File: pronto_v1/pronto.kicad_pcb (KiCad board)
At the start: 2 copper layers, 53.3 x 81.3 mm, 480 parts

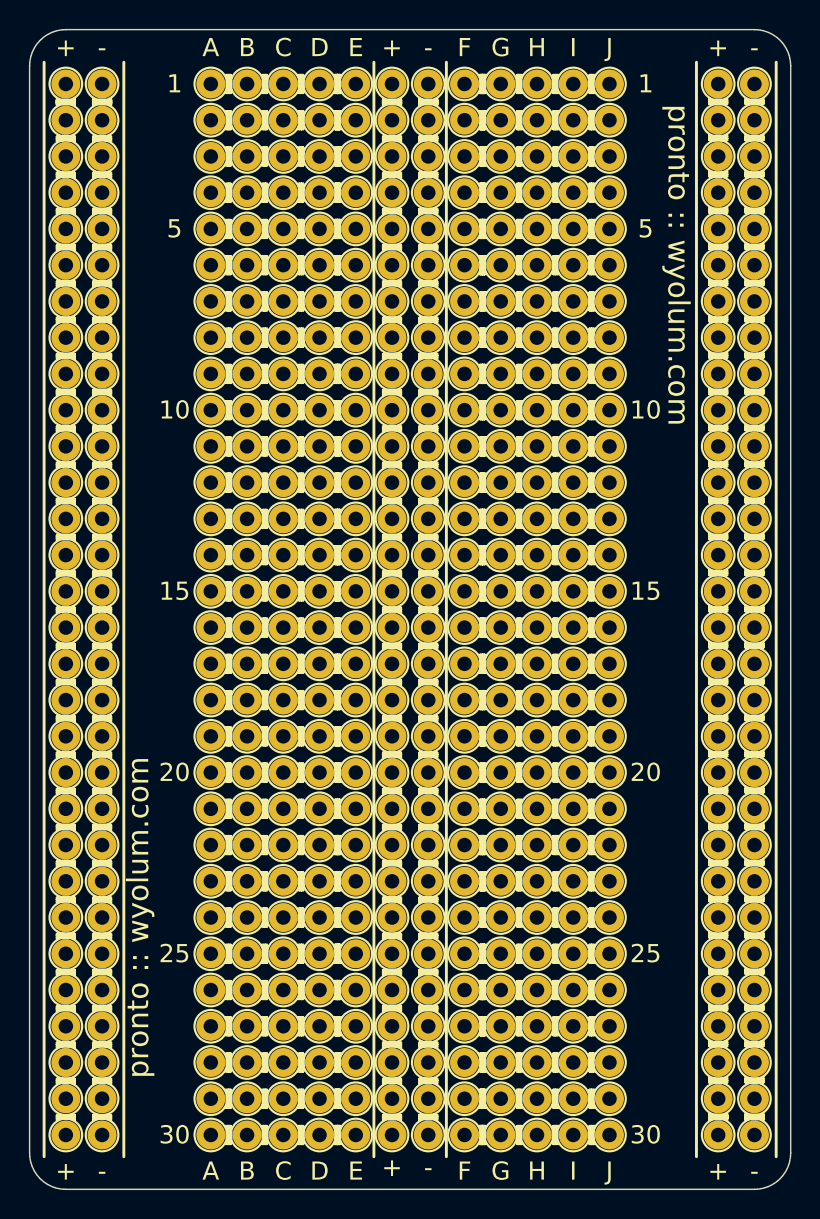
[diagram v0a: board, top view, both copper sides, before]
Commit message: updated Maker's Asylum version and added Makerville version
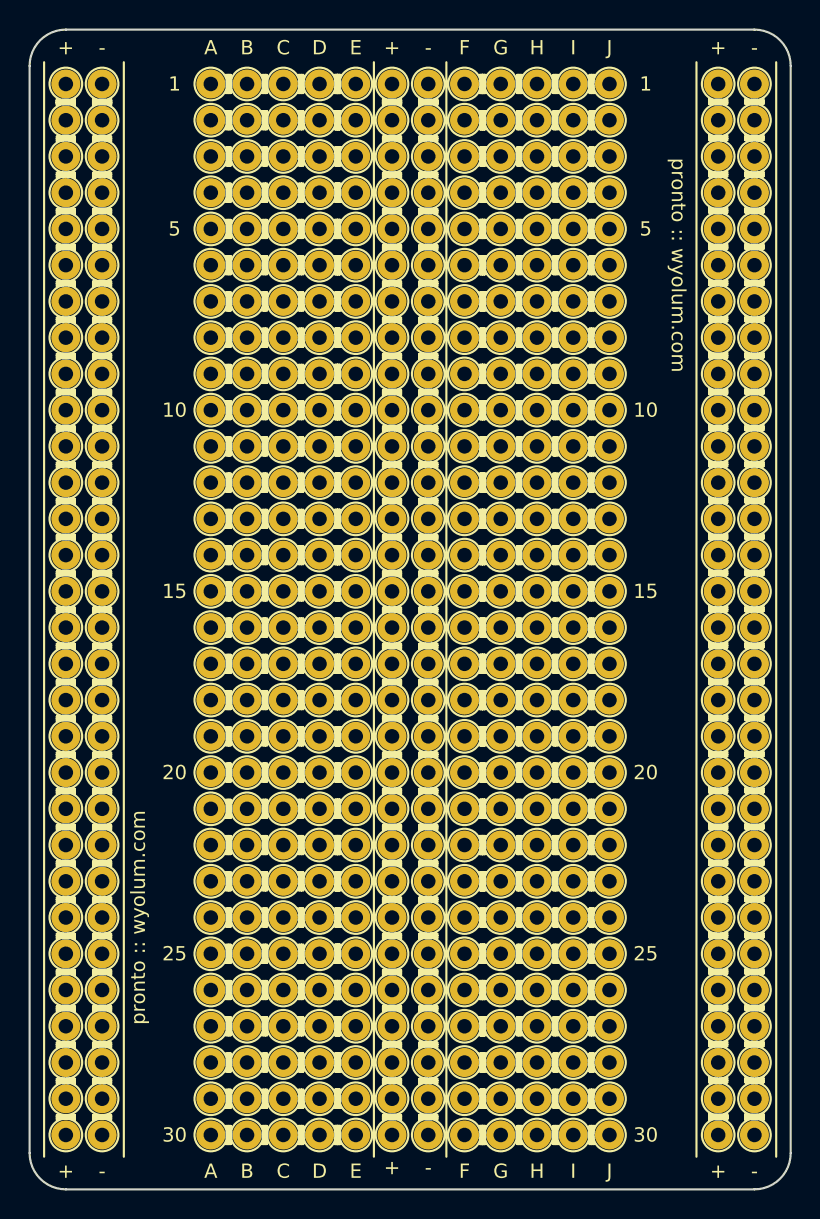
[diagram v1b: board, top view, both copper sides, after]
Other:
- net class 15mil removed
- net class 20mil removed
- net class Default removed

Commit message: two Makerville versions
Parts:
- removed the 1pin at (139.7, 116.8)
- removed the 1pin at (142.2, 116.8)
- removed the 1pin at (94.0, 116.8)
- removed the 1pin at (96.5, 116.8)
- moved 1pin 1.27 mm to (139.7, 97.8)
- moved 1pin 1.27 mm to (142.2, 97.8)
- moved 1pin 1.27 mm to (142.2, 85.1)
- moved 1pin 1.27 mm to (139.7, 85.1)
- moved 1pin 1.27 mm to (139.7, 80.0)
- moved 1pin 1.27 mm to (142.2, 80.0)
- moved 1pin 1.27 mm to (94.0, 102.9)
- moved 1pin 1.27 mm to (96.5, 102.9)
- moved 1pin 1.27 mm to (139.7, 102.9)
- moved 1pin 1.27 mm to (142.2, 102.9)
- moved 1pin 1.27 mm to (139.7, 74.9)
- moved 1pin 1.27 mm to (142.2, 74.9)
- moved 1pin 1.27 mm to (94.0, 74.9)
- moved 1pin 1.27 mm to (96.5, 74.9)
- moved 1pin 1.27 mm to (94.0, 80.0)
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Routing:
- net (no net): track 1056.6 -> 1051.6 mm
